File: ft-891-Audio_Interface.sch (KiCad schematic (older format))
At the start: 13 parts, among them J1 Mic Cable, J2 Audio In, J3 Headset, J4 PTT, J5 Aviation Audio Jack, J6 Aviation Mic Jack

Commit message: First pass at routing and layout
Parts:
- C3, C4: footprint (none) -> Capacitors_SMD:CP_Elec_8x10
- J2, J3, J4: footprint BVH_Connectors_Misc:SJ-43516-SMT-TRRS_Audio_Jack_w_switch -> BVH_Connectors_Misc:SJ-43515RS-SMT-TR
- J5: value Aviation Audio Jack -> Av Audio Jack
- J6: value Aviation Mic Jack -> Av Mic Jack
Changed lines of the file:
@@
 F 0 "J2" H 1882 3725 50  0000 C CNN
 F 1 "Audio In" H 1882 3634 50  0000 C CNN
-F 2 "BVH_Connectors_Misc:SJ-43516-SMT-TRRS_Audio_Jack_w_switch" H 1900 3300 50  0001 C CNN
+F 2 "BVH_Connectors_Misc:SJ-43515RS-SMT-TR" H 1900 3300 50  0001 C CNN
 F 3 "~" H 1900 3300 50  0001 C CNN
 	1    1950 3300
@@
 F 0 "J3" H 9420 3483 50  0000 R CNN
 F 1 "Headset" H 9850 3950 50  0000 R CNN
-F 2 "BVH_Connectors_Misc:SJ-43516-SMT-TRRS_Audio_Jack_w_switch" H 9750 3600 50  0001 C CNN
+F 2 "BVH_Connectors_Misc:SJ-43515RS-SMT-TR" H 9750 3600 50  0001 C CNN
 F 3 "~" H 9750 3600 50  0001 C CNN
 	1    9800 3600
@@
 F 0 "J4" H 9420 4583 50  0000 R CNN
 F 1 "PTT" H 9700 5050 50  0000 R CNN
-F 2 "BVH_Connectors_Misc:SJ-43516-SMT-TRRS_Audio_Jack_w_switch" H 9750 4700 50  0001 C CNN
+F 2 "BVH_Connectors_Misc:SJ-43515RS-SMT-TR" H 9750 4700 50  0001 C CNN
 F 3 "~" H 9750 4700 50  0001 C CNN
 	1    9800 4700
@@
 P 10000 1050
 F 0 "J5" H 10080 1092 50  0000 L CNN
-F 1 "Aviation Audio Jack" H 9450 800 50  0000 L CNN
+F 1 "Av Audio Jack" H 9450 800 50  0000 L CNN
 F 2 "Pin_Headers:Pin_Header_Straight_1x03_Pitch2.54mm" H 10000 1050 50  0001 C CNN
 F 3 "~" H 10000 1050 50  0001 C CNN
@@
 P 10000 1750
 F 0 "J6" H 10080 1792 50  0000 L CNN
-F 1 "Aviation Mic Jack" H 9450 1500 50  0000 L CNN
+F 1 "Av Mic Jack" H 9450 1500 50  0000 L CNN
 F 2 "Pin_Headers:Pin_Header_Straight_1x03_Pitch2.54mm" H 10000 1750 50  0001 C CNN
 F 3 "~" H 10000 1750 50  0001 C CNN
@@
 F 0 "C3" V 5605 2350 50  0000 C CNN
 F 1 "100 uF" V 5514 2350 50  0000 C CNN
-F 2 "" H 5388 2200 50  0001 C CNN
+F 2 "Capacitors_SMD:CP_Elec_8x10" H 5388 2200 50  0001 C CNN
 F 3 "~" H 5350 2350 50  0001 C CNN
 	1    5350 2350
@@
 F 0 "C4" V 5395 2350 50  0000 C CNN
 F 1 "100 uF" V 5486 2350 50  0000 C CNN
-F 2 "" H 5688 2200 50  0001 C CNN
+F 2 "Capacitors_SMD:CP_Elec_8x10" H 5688 2200 50  0001 C CNN
 F 3 "~" H 5650 2350 50  0001 C CNN
 	1    5650 2350

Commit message: Add expansion header and NPTH for mounting
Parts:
- added J7: Audio Breakout, Pin_Headers:Pin_Header_Straight_2x04_Pitch2.54mm, symbol Connector_Generic:Conn_02x04_Odd_Even
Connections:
- net +5V: now also J7.7 (Pin_7)
- net Audio_In_L: now also J7.3 (Pin_3); no longer J3.2 (T), J5.1 (Pin_1)
- net Audio_In_R: now also J7.5 (Pin_5); no longer J3.3 (R1), J5.2 (Pin_2)
- net Av_Mic: now also J7.1 (Pin_1); no longer C2.1, C3.1, R1.2
- net GND: now also J7.8 (Pin_8)
- new net Audio_Out_L: J3.2 (T), J5.1 (Pin_1), J7.4 (Pin_4)
- new net Audio_Out_R: J3.3 (R1), J5.2 (Pin_2), J7.6 (Pin_6)
- new net Mic_In: C2.1, C3.1, J7.2 (Pin_2), R1.2
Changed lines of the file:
@@
 $EndComp
 Wire Wire Line
-	4400 2350 4600 2350
+	6600 4350 6800 4350
 $Comp
 L Device:C C2
@@
 	1800 5950 1650 5950
 Wire Wire Line
-	4400 2150 4600 2150
-Wire Wire Line
-	4600 2150 4600 2350
-Connection ~ 4600 2350
+	6600 4150 6800 4150
 Wire Wire Line
 	4600 2350 4950 2350
@@
 Text GLabel 2300 2100 2    50   Input ~ 0
 Mic
-Text GLabel 5350 5600 0    50   Input ~ 0
+Text GLabel 6950 4450 0    50   Input ~ 0
 Audio_In_L
-Text GLabel 5350 5800 0    50   Input ~ 0
+Text GLabel 6950 4550 0    50   Input ~ 0
 Audio_In_R
 Text GLabel 6000 5550 2    50   Input ~ 0
@@
 Text GLabel 6000 5850 2    50   Input ~ 0
 Headset_Out_R
-Text GLabel 4400 2150 0    50   Input ~ 0
+Text GLabel 6600 4150 0    50   Input ~ 0
 Av_Mic
-Text GLabel 4400 2350 0    50   Input ~ 0
+Text GLabel 6600 4350 0    50   Input ~ 0
 Headset_Mic
 Text GLabel 6500 2500 2    50   Input ~ 0
@@
 Text Notes 10650 7650 0    50   ~ 0
 2019-11-18
+$Comp
+L Connector_Generic:Conn_02x04_Odd_Even J7
+U 1 1 5DF1ABE0
+P 7150 4450
+F 0 "J7" H 7200 4767 50  0000 C CNN
+F 1 "Audio Breakout" H 7200 4676 50  0000 C CNN
+F 2 "Pin_Headers:Pin_Header_Straight_2x04_Pitch2.54mm" H 7150 4450 50  0001 C CNN
+F 3 "~" H 7150 4450 50  0001 C CNN
+	1    7150 4450
+	1    0    0    -1
+$EndComp
+Text GLabel 7450 4350 2    50   Input ~ 0
+Mic_In
+Text GLabel 7450 4450 2    50   Input ~ 0
+Audio_Out_L
+Text GLabel 7450 4550 2    50   Input ~ 0
+Audio_Out_R
+Text GLabel 5350 5600 0    50   Input ~ 0
+Audio_Out_L
+Text GLabel 5350 5800 0    50   Input ~ 0
+Audio_Out_R
+Wire Wire Line
+	6800 4150 6800 4350
+Wire Wire Line
+	6800 4350 6950 4350
+Connection ~ 6800 4350
+Text GLabel 4600 2350 0    50   Input ~ 0
+Mic_In
+$Comp
+L power:GND #PWR0101
+U 1 1 5DF2A88A
+P 7700 4650
+F 0 "#PWR0101" H 7700 4400 50  0001 C CNN
+F 1 "GND" H 7705 4477 50  0000 C CNN
+F 2 "" H 7700 4650 50  0001 C CNN
+F 3 "" H 7700 4650 50  0001 C CNN
+	1    7700 4650
+	1    0    0    -1
+$EndComp
+Wire Wire Line
+	7450 4650 7700 4650
+$Comp
+L power:+5V #PWR0102
+U 1 1 5DF2B794
+P 6300 4650
+F 0 "#PWR0102" H 6300 4500 50  0001 C CNN
+F 1 "+5V" H 6315 4823 50  0000 C CNN
+F 2 "" H 6300 4650 50  0001 C CNN
+F 3 "" H 6300 4650 50  0001 C CNN
+	1    6300 4650
+	1    0    0    -1
+$EndComp
+Wire Wire Line
+	6300 4650 6950 4650
 $EndSCHEMATC

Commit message: WIP
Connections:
- net GND: now also J1.5; no longer J1.4
- net Mic: now also J1.4; no longer J1.5
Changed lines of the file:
@@
 $EndDescr
-$Comp
-L Connector:RJ45_Shielded J1
-U 1 1 5DE76DAC
-P 1900 2200
-F 0 "J1" H 1957 2867 50  0000 C CNN
-F 1 "Mic Cable" H 1957 2776 50  0000 C CNN
-F 2 "BVH_Connectors_Misc:Molex_0855055002_RJ-45_Jack_Shielded_Yaesu_Numbering" V 1900 2225 50  0001 C CNN
-F 3 "~" V 1900 2225 50  0001 C CNN
-	1    1900 2200
-	1    0    0    -1
-$EndComp
 $Comp
 L BVH_Connectors_Misc:AudioJack4_SwitchTR J2
@@
 Wire Wire Line
 	2700 2400 2700 2200
-Connection ~ 2700 2200
-Wire Wire Line
-	2700 2200 2300 2200
 $Comp
 L power:+5V #PWR04
@@
 Text GLabel 2300 2300 2    50   Input ~ 0
 PTT
-Text GLabel 2300 2100 2    50   Input ~ 0
+Text GLabel 2300 2200 2    50   Input ~ 0
 Mic
 Text GLabel 6950 4450 0    50   Input ~ 0
@@
 Wire Wire Line
 	6300 4650 6950 4650
+$Comp
+L Connector:RJ45_Shielded J1
+U 1 1 5DE76DAC
+P 1900 2200
+F 0 "J1" H 1957 2867 50  0000 C CNN
+F 1 "Mic Cable" H 1957 2776 50  0000 C CNN
+F 2 "BVH_Connectors_Misc:Molex_0855055002_RJ-45_Jack_Shielded_Yaesu_Numbering" V 1900 2225 50  0001 C CNN
+F 3 "~" V 1900 2225 50  0001 C CNN
+	1    1900 2200
+	1    0    0    -1
+$EndComp
+Wire Wire Line
+	2700 2200 2700 2100
+Wire Wire Line
+	2700 2100 2300 2100
+Connection ~ 2700 2200
 $EndSCHEMATC

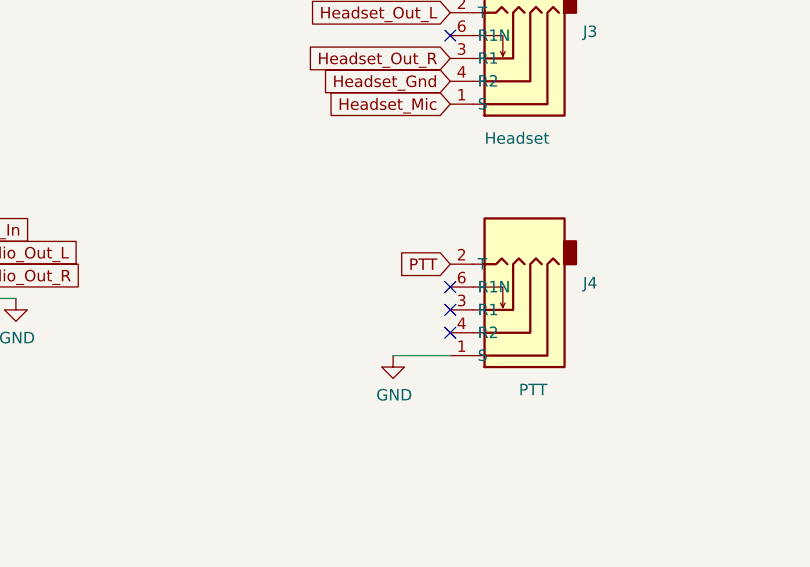
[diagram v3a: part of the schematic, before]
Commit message: FT-891 interface v2 - Fix earlier mistakes, larger board, mounting holes
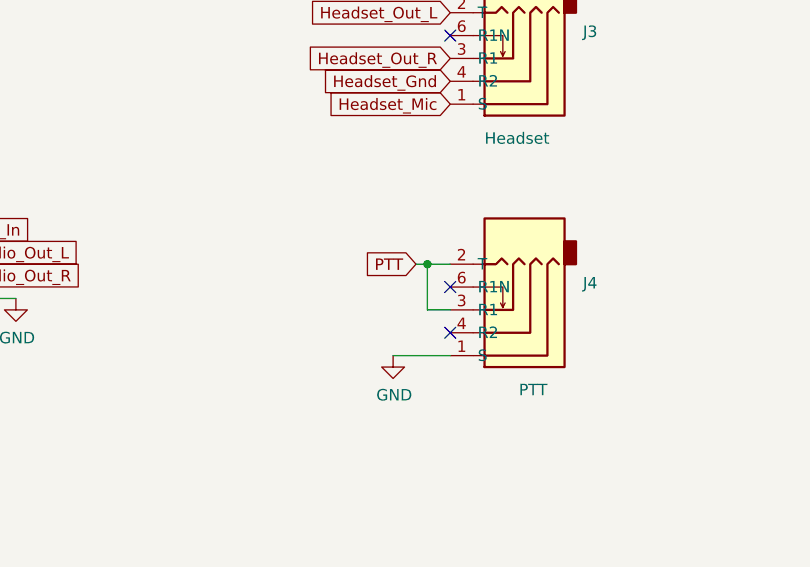
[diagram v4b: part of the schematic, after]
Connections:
- net PTT: now also J4.3 (R1)
- no-connect marks 9 -> 8
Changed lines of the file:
@@
 EESchema Schematic File Version 4
-LIBS:ft-891-Audio_Interface-cache
 EELAYER 30 0
 EELAYER END
@@
 	1650 5650 1800 5650
 Connection ~ 1650 5650
-NoConn ~ 9600 4700
 NoConn ~ 9600 4800
 $Comp
@@
 Text GLabel 9600 3800 0    50   Input ~ 0
 Headset_Mic
-Text GLabel 9600 4500 0    50   Input ~ 0
+Text GLabel 9450 4500 0    50   Input ~ 0
 PTT
 Text GLabel 1800 5500 2    50   Input ~ 0
@@
 	2700 2100 2300 2100
 Connection ~ 2700 2200
+Wire Wire Line
+	9450 4500 9500 4500
+Wire Wire Line
+	9500 4500 9500 4700
+Wire Wire Line
+	9500 4700 9600 4700
+Connection ~ 9500 4500
+Wire Wire Line
+	9500 4500 9600 4500
 $EndSCHEMATC
